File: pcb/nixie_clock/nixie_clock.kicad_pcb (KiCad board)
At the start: 4 copper layers, 0 parts

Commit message: schematic finalisation, footprint assignment and start on placeing components in layout.
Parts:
- added C1: 10u, Capacitor_SMD:C_1210_3225Metric, F.Cu at (165.8, 121.5)
- added C2: 100n, Capacitor_SMD:C_0805_2012Metric, F.Cu at (179.9, 124.5)
- added C3: 560p, Capacitor_SMD:C_0603_1608Metric, F.Cu at (161.0, 110.7)
- added C4: 150n, Capacitor_SMD:C_0603_1608Metric, F.Cu at (161.0, 113.2)
- added C5: 4u7, Capacitor_SMD:C_0603_1608Metric, F.Cu at (161.0, 115.8)
- added C6: 2u2, Capacitor_SMD:C_2220_5750Metric, F.Cu at (174.3, 113.0)
- added C7: 100n, Capacitor_SMD:C_1812_4532Metric, F.Cu at (166.5, 112.0)
- added C8: 10u, Capacitor_SMD:C_1210_3225Metric, F.Cu at (165.8, 125.8)
- added D1: D, Capacitor_SMD:C_1812_4532Metric, F.Cu at (166.5, 116.9)
- added Q1: Q_NMOS_GDS, Package_TO_SOT_SMD:LFPAK56, F.Cu at (174.3, 119.7)
- added R1: 7K87, Resistor_SMD:R_0603_1608Metric, F.Cu at (62.0, 84.6)
- added R10: 1K, Resistor_SMD:R_0603_1608Metric, F.Cu at (70.0, 87.1)
- added R11: 1K, Resistor_SMD:R_0603_1608Metric, F.Cu at (70.0, 89.6)
- added R12: 1K, Resistor_SMD:R_0603_1608Metric, F.Cu at (70.0, 92.1)
- added R13: 7K87, Resistor_SMD:R_0603_1608Metric, F.Cu at (84.3, 86.5)
- added R14: 1K, Resistor_SMD:R_0603_1608Metric, F.Cu at (84.3, 89.0)
- added R15: 1K, Resistor_SMD:R_0603_1608Metric, F.Cu at (84.3, 91.5)
- added R16: 1K, Resistor_SMD:R_0603_1608Metric, F.Cu at (84.3, 94.0)
- added R17: 1K, Resistor_SMD:R_0603_1608Metric, F.Cu at (88.3, 86.5)
- added R18: 1K, Resistor_SMD:R_0603_1608Metric, F.Cu at (88.3, 89.0)
- added R19: 7K87, Resistor_SMD:R_0603_1608Metric, F.Cu at (88.3, 91.5)
- added R2: 1K, Resistor_SMD:R_0603_1608Metric, F.Cu at (62.0, 87.1)
- added R20: 1K, Resistor_SMD:R_0603_1608Metric, F.Cu at (88.3, 94.0)
- added R21: 1K, Resistor_SMD:R_0603_1608Metric, F.Cu at (92.3, 86.5)
- added R22: 1K, Resistor_SMD:R_0603_1608Metric, F.Cu at (92.3, 89.0)
- added R23: 1K, Resistor_SMD:R_0603_1608Metric, F.Cu at (92.3, 91.5)
- added R24: 1K, Resistor_SMD:R_0603_1608Metric, F.Cu at (92.3, 94.0)
- added R25: 7K87, Resistor_SMD:R_0603_1608Metric, F.Cu at (105.8, 83.5)
- added R26: 1K, Resistor_SMD:R_0603_1608Metric, F.Cu at (105.8, 86.0)
- added R27: 1K, Resistor_SMD:R_0603_1608Metric, F.Cu at (105.8, 88.5)
- added R28: 1K, Resistor_SMD:R_0603_1608Metric, F.Cu at (105.8, 91.0)
- added R29: 1K, Resistor_SMD:R_0603_1608Metric, F.Cu at (109.8, 83.5)
- added R3: 1K, Resistor_SMD:R_0603_1608Metric, F.Cu at (62.0, 89.6)
- added R30: 1K, Resistor_SMD:R_0603_1608Metric, F.Cu at (109.8, 86.0)
- added R31: 7K87, Resistor_SMD:R_0603_1608Metric, F.Cu at (109.8, 88.5)
- added R32: 1K, Resistor_SMD:R_0603_1608Metric, F.Cu at (109.8, 91.0)
- added R33: 1K, Resistor_SMD:R_0603_1608Metric, F.Cu at (113.8, 83.5)
- added R34: 1K, Resistor_SMD:R_0603_1608Metric, F.Cu at (113.8, 86.0)
- added R35: 1K, Resistor_SMD:R_0603_1608Metric, F.Cu at (113.8, 88.5)
- added R36: 1K, Resistor_SMD:R_0603_1608Metric, F.Cu at (113.8, 91.0)
- added R37: 7K87, Resistor_SMD:R_0603_1608Metric, F.Cu at (129.0, 86.2)
- added R38: 1K, Resistor_SMD:R_0603_1608Metric, F.Cu at (129.0, 88.7)
- added R39: 1K, Resistor_SMD:R_0603_1608Metric, F.Cu at (129.0, 91.3)
- added R4: 1K, Resistor_SMD:R_0603_1608Metric, F.Cu at (62.0, 92.1)
- added R40: 1K, Resistor_SMD:R_0603_1608Metric, F.Cu at (129.0, 93.8)
- added R41: 1K, Resistor_SMD:R_0603_1608Metric, F.Cu at (133.0, 86.2)
- added R42: 1K, Resistor_SMD:R_0603_1608Metric, F.Cu at (133.0, 88.7)
- added R43: 7K87, Resistor_SMD:R_0603_1608Metric, F.Cu at (133.0, 91.3)
- added R44: 1K, Resistor_SMD:R_0603_1608Metric, F.Cu at (133.0, 93.8)
- added R45: 1K, Resistor_SMD:R_0603_1608Metric, F.Cu at (137.0, 86.2)
- added R46: 1K, Resistor_SMD:R_0603_1608Metric, F.Cu at (137.0, 88.7)
- added R47: 1K, Resistor_SMD:R_0603_1608Metric, F.Cu at (137.0, 91.3)
- added R48: 1K, Resistor_SMD:R_0603_1608Metric, F.Cu at (137.0, 93.8)
- added R49: 7K87, Resistor_SMD:R_0603_1608Metric, F.Cu at (152.0, 84.7)
- added R5: 1K, Resistor_SMD:R_0603_1608Metric, F.Cu at (66.0, 84.6)
- added R50: 1K, Resistor_SMD:R_0603_1608Metric, F.Cu at (152.0, 87.2)
- added R51: 1K, Resistor_SMD:R_0603_1608Metric, F.Cu at (152.0, 89.8)
- added R52: 1K, Resistor_SMD:R_0603_1608Metric, F.Cu at (152.0, 92.3)
- added R53: 1K, Resistor_SMD:R_0603_1608Metric, F.Cu at (156.0, 84.7)
- added R54: 1K, Resistor_SMD:R_0603_1608Metric, F.Cu at (156.0, 87.2)
- added R55: 7K87, Resistor_SMD:R_0603_1608Metric, F.Cu at (156.0, 89.8)
- added R56: 1K, Resistor_SMD:R_0603_1608Metric, F.Cu at (156.0, 92.3)
- added R57: 1K, Resistor_SMD:R_0603_1608Metric, F.Cu at (160.0, 84.7)
- added R58: 1K, Resistor_SMD:R_0603_1608Metric, F.Cu at (160.0, 87.2)
- added R59: 1K, Resistor_SMD:R_0603_1608Metric, F.Cu at (160.0, 89.8)
- added R6: 1K, Resistor_SMD:R_0603_1608Metric, F.Cu at (66.0, 87.1)
- added R60: 1K, Resistor_SMD:R_0603_1608Metric, F.Cu at (160.0, 92.3)
- added R61: 10m, Resistor_SMD:R_0805_2012Metric, F.Cu at (179.9, 127.5)
- added R62: 1M6, Resistor_SMD:R_0603_1608Metric, F.Cu at (161.0, 118.3)
- added R63: 13K, Resistor_SMD:R_0603_1608Metric, F.Cu at (161.0, 120.8)
- added R64: 20R, Resistor_SMD:R_0603_1608Metric, F.Cu at (161.0, 123.3)
- added R65: 300K, Resistor_SMD:R_0603_1608Metric, F.Cu at (161.0, 125.8)
- added R66: 7K87, Resistor_SMD:R_0603_1608Metric, F.Cu at (173.5, 44.0)
- added R67: 1K, Resistor_SMD:R_0603_1608Metric, F.Cu at (170.5, 45.5)
- added R68: 1K, Resistor_SMD:R_0603_1608Metric, F.Cu at (168.0, 49.5)
- added R69: 1K, Resistor_SMD:R_0603_1608Metric, F.Cu at (171.0, 63.5)
- added R7: 7K87, Resistor_SMD:R_0603_1608Metric, F.Cu at (66.0, 89.6)
- added R70: 1K, Resistor_SMD:R_0603_1608Metric, F.Cu at (174.5, 71.0)
- added R71: 1K, Resistor_SMD:R_0603_1608Metric, F.Cu at (179.5, 71.7)
- added R72: 86K6, Resistor_SMD:R_0603_1608Metric, F.Cu at (161.0, 128.3)
- added R73: 7K87, Resistor_SMD:R_0603_1608Metric, F.Cu at (180.3, 42.0)
- added R74: 1K, Resistor_SMD:R_0603_1608Metric, F.Cu at (187.0, 43.3)
- added R75: 1K, Resistor_SMD:R_0603_1608Metric, F.Cu at (191.0, 46.5)
- added R76: 1K, Resistor_SMD:R_0603_1608Metric, F.Cu at (190.0, 66.0)
- added R77: 1K, Resistor_SMD:R_0603_1608Metric, F.Cu at (187.0, 69.2)
- added R78: 1K, Resistor_SMD:R_0603_1608Metric, F.Cu at (183.5, 71.7)
- added R8: 1K, Resistor_SMD:R_0603_1608Metric, F.Cu at (66.0, 92.1)
- added R9: 1K, Resistor_SMD:R_0603_1608Metric, F.Cu at (70.0, 84.6)
- added T1: 750312367, 750312367:750312367, F.Cu at (170.3, 102.8)
- added U1: MSD42WT1G, footprints:SOT-323-3_2P2X1P35_ONS, F.Cu at (62.0, 69.6)
- added U10: MSD42WT1G, footprints:SOT-323-3_2P2X1P35_ONS, F.Cu at (65.8, 80.4)
- added U11: MSD42WT1G, footprints:SOT-323-3_2P2X1P35_ONS, F.Cu at (69.7, 80.4)
- added U12: MSD42WT1G, footprints:SOT-323-3_2P2X1P35_ONS, F.Cu at (73.6, 80.4)
- added U13: PCA9685BS, Package_DFN_QFN:QFN-28-1EP_6x6mm_P0.65mm_EP4.25x4.25mm, F.Cu at (237.1, 129.7)
- added U14: PicoW, RPi_Pico:RPi_PicoW_SMD, F.Cu at (71.0, 127.5)
- added U15: PCA9685BS, Package_DFN_QFN:QFN-28-1EP_6x6mm_P0.65mm_EP4.25x4.25mm, F.Cu at (226.8, 129.7)
- added U16: MSD42WT1G, footprints:SOT-323-3_2P2X1P35_ONS, F.Cu at (84.3, 71.5)
- added U17: MSD42WT1G, footprints:SOT-323-3_2P2X1P35_ONS, F.Cu at (88.1, 71.5)
- added U18: MSD42WT1G, footprints:SOT-323-3_2P2X1P35_ONS, F.Cu at (92.0, 71.5)
- added U19: MSD42WT1G, footprints:SOT-323-3_2P2X1P35_ONS, F.Cu at (95.9, 71.5)
- added U2: MSD42WT1G, footprints:SOT-323-3_2P2X1P35_ONS, F.Cu at (65.8, 69.6)
- added U20: MSD42WT1G, footprints:SOT-323-3_2P2X1P35_ONS, F.Cu at (84.3, 76.9)
- added U21: MSD42WT1G, footprints:SOT-323-3_2P2X1P35_ONS, F.Cu at (88.1, 76.9)
- added U22: MSD42WT1G, footprints:SOT-323-3_2P2X1P35_ONS, F.Cu at (92.0, 76.9)
- added U23: MSD42WT1G, footprints:SOT-323-3_2P2X1P35_ONS, F.Cu at (95.9, 76.9)
- added U24: MSD42WT1G, footprints:SOT-323-3_2P2X1P35_ONS, F.Cu at (84.3, 82.2)
- added U25: MSD42WT1G, footprints:SOT-323-3_2P2X1P35_ONS, F.Cu at (88.1, 82.2)
- added U26: MSD42WT1G, footprints:SOT-323-3_2P2X1P35_ONS, F.Cu at (92.0, 82.2)
- added U27: MSD42WT1G, footprints:SOT-323-3_2P2X1P35_ONS, F.Cu at (95.9, 82.2)
- added U28: PCA9685BS, Package_DFN_QFN:QFN-28-1EP_6x6mm_P0.65mm_EP4.25x4.25mm, F.Cu at (199.5, 129.7)
- added U29: MSD42WT1G, footprints:SOT-323-3_2P2X1P35_ONS, F.Cu at (105.7, 68.5)
- added U3: MSD42WT1G, footprints:SOT-323-3_2P2X1P35_ONS, F.Cu at (69.7, 69.6)
- added U30: MSD42WT1G, footprints:SOT-323-3_2P2X1P35_ONS, F.Cu at (109.6, 68.5)
- added U31: MSD42WT1G, footprints:SOT-323-3_2P2X1P35_ONS, F.Cu at (113.5, 68.5)
- added U32: MSD42WT1G, footprints:SOT-323-3_2P2X1P35_ONS, F.Cu at (117.3, 68.5)
- added U33: MSD42WT1G, footprints:SOT-323-3_2P2X1P35_ONS, F.Cu at (105.7, 73.9)
- added U34: MSD42WT1G, footprints:SOT-323-3_2P2X1P35_ONS, F.Cu at (109.6, 73.9)
- added U35: MSD42WT1G, footprints:SOT-323-3_2P2X1P35_ONS, F.Cu at (113.5, 73.9)
- added U36: MSD42WT1G, footprints:SOT-323-3_2P2X1P35_ONS, F.Cu at (117.3, 73.9)
- added U37: MSD42WT1G, footprints:SOT-323-3_2P2X1P35_ONS, F.Cu at (105.7, 79.3)
- added U38: MSD42WT1G, footprints:SOT-323-3_2P2X1P35_ONS, F.Cu at (109.6, 79.3)
- added U39: MSD42WT1G, footprints:SOT-323-3_2P2X1P35_ONS, F.Cu at (113.5, 79.3)
- added U4: MSD42WT1G, footprints:SOT-323-3_2P2X1P35_ONS, F.Cu at (73.6, 69.6)
- added U40: MSD42WT1G, footprints:SOT-323-3_2P2X1P35_ONS, F.Cu at (117.3, 79.3)
- added U41: PCA9685BS, Package_DFN_QFN:QFN-28-1EP_6x6mm_P0.65mm_EP4.25x4.25mm, F.Cu at (189.2, 129.7)
- added U42: MSD42WT1G, footprints:SOT-323-3_2P2X1P35_ONS, F.Cu at (129.0, 71.3)
- added U43: MSD42WT1G, footprints:SOT-323-3_2P2X1P35_ONS, F.Cu at (132.8, 71.3)
- added U44: MSD42WT1G, footprints:SOT-323-3_2P2X1P35_ONS, F.Cu at (136.7, 71.3)
- added U45: MSD42WT1G, footprints:SOT-323-3_2P2X1P35_ONS, F.Cu at (140.6, 71.3)
- added U46: MSD42WT1G, footprints:SOT-323-3_2P2X1P35_ONS, F.Cu at (129.0, 76.6)
- added U47: MSD42WT1G, footprints:SOT-323-3_2P2X1P35_ONS, F.Cu at (132.8, 76.6)
- added U48: MSD42WT1G, footprints:SOT-323-3_2P2X1P35_ONS, F.Cu at (136.7, 76.6)
- added U49: MSD42WT1G, footprints:SOT-323-3_2P2X1P35_ONS, F.Cu at (140.6, 76.6)
- added U5: MSD42WT1G, footprints:SOT-323-3_2P2X1P35_ONS, F.Cu at (62.0, 75.0)
- added U50: MSD42WT1G, footprints:SOT-323-3_2P2X1P35_ONS, F.Cu at (129.0, 82.0)
- added U51: MSD42WT1G, footprints:SOT-323-3_2P2X1P35_ONS, F.Cu at (132.8, 82.0)
- added U52: MSD42WT1G, footprints:SOT-323-3_2P2X1P35_ONS, F.Cu at (136.7, 82.0)
- added U53: MSD42WT1G, footprints:SOT-323-3_2P2X1P35_ONS, F.Cu at (140.6, 82.0)
- added U54: PCA9685BS, Package_DFN_QFN:QFN-28-1EP_6x6mm_P0.65mm_EP4.25x4.25mm, F.Cu at (209.8, 129.7)
- added U55: MSD42WT1G, footprints:SOT-323-3_2P2X1P35_ONS, F.Cu at (152.0, 69.8)
- added U56: MSD42WT1G, footprints:SOT-323-3_2P2X1P35_ONS, F.Cu at (155.8, 69.8)
- added U57: MSD42WT1G, footprints:SOT-323-3_2P2X1P35_ONS, F.Cu at (159.7, 69.8)
- added U58: MSD42WT1G, footprints:SOT-323-3_2P2X1P35_ONS, F.Cu at (163.6, 69.8)
- added U59: MSD42WT1G, footprints:SOT-323-3_2P2X1P35_ONS, F.Cu at (152.0, 75.1)
- added U6: MSD42WT1G, footprints:SOT-323-3_2P2X1P35_ONS, F.Cu at (65.8, 75.0)
- added U60: MSD42WT1G, footprints:SOT-323-3_2P2X1P35_ONS, F.Cu at (155.8, 75.1)
- added U61: MSD42WT1G, footprints:SOT-323-3_2P2X1P35_ONS, F.Cu at (159.7, 75.1)
- added U62: MSD42WT1G, footprints:SOT-323-3_2P2X1P35_ONS, F.Cu at (163.6, 75.1)
- added U63: MSD42WT1G, footprints:SOT-323-3_2P2X1P35_ONS, F.Cu at (152.0, 80.5)
- added U64: MSD42WT1G, footprints:SOT-323-3_2P2X1P35_ONS, F.Cu at (155.8, 80.5)
- added U65: MSD42WT1G, footprints:SOT-323-3_2P2X1P35_ONS, F.Cu at (159.7, 80.5)
- added U66: MSD42WT1G, footprints:SOT-323-3_2P2X1P35_ONS, F.Cu at (177.3, 45.0)
- added U67: MSD42WT1G, footprints:SOT-323-3_2P2X1P35_ONS, F.Cu at (171.2, 49.0)
- added U68: MSD42WT1G, footprints:SOT-323-3_2P2X1P35_ONS, F.Cu at (168.7, 53.5)
- added U69: MSD42WT1G, footprints:SOT-323-3_2P2X1P35_ONS, F.Cu at (168.7, 60.0)
- added U7: MSD42WT1G, footprints:SOT-323-3_2P2X1P35_ONS, F.Cu at (69.7, 75.0)
- added U70: MSD42WT1G, footprints:SOT-323-3_2P2X1P35_ONS, F.Cu at (173.7, 67.0)
- added U71: MSD42WT1G, footprints:SOT-323-3_2P2X1P35_ONS, F.Cu at (178.7, 68.0)
- added U72: MSD42WT1G, footprints:SOT-323-3_2P2X1P35_ONS, F.Cu at (183.5, 45.0)
- added U73: MSD42WT1G, footprints:SOT-323-3_2P2X1P35_ONS, F.Cu at (187.7, 47.5)
- added U74: MSD42WT1G, footprints:SOT-323-3_2P2X1P35_ONS, F.Cu at (191.2, 51.0)
- added U75: MSD42WT1G, footprints:SOT-323-3_2P2X1P35_ONS, F.Cu at (189.3, 62.0)
- added U76: MSD42WT1G, footprints:SOT-323-3_2P2X1P35_ONS, F.Cu at (186.3, 65.0)
- added U77: MSD42WT1G, footprints:SOT-323-3_2P2X1P35_ONS, F.Cu at (182.3, 68.0)
- added U78: MSD42WT1G, footprints:SOT-323-3_2P2X1P35_ONS, F.Cu at (163.6, 80.5)
- added U79: LT3759EMSE-TRPBF, LT3759EMSE:MSOP-12_MSE_LIT, F.Cu at (173.8, 125.9)
- added U8: MSD42WT1G, footprints:SOT-323-3_2P2X1P35_ONS, F.Cu at (73.6, 75.0)
- added U9: MSD42WT1G, footprints:SOT-323-3_2P2X1P35_ONS, F.Cu at (62.0, 80.4)
- added V1: IN14, Nixie_Stuff:IN14, B.Cu at (66.8, 57.7)
- added V2: IN14, Nixie_Stuff:IN14, B.Cu at (88.9, 57.5)
- added V3: IN14, Nixie_Stuff:IN14, B.Cu at (108.9, 56.5)
- added V4: IN14, Nixie_Stuff:IN14, B.Cu at (134.1, 56.5)
- added V5: IN14, Nixie_Stuff:IN14, B.Cu at (156.0, 56.2)
- added V6: IN14, Nixie_Stuff:IN14, B.Cu at (180.0, 56.0)

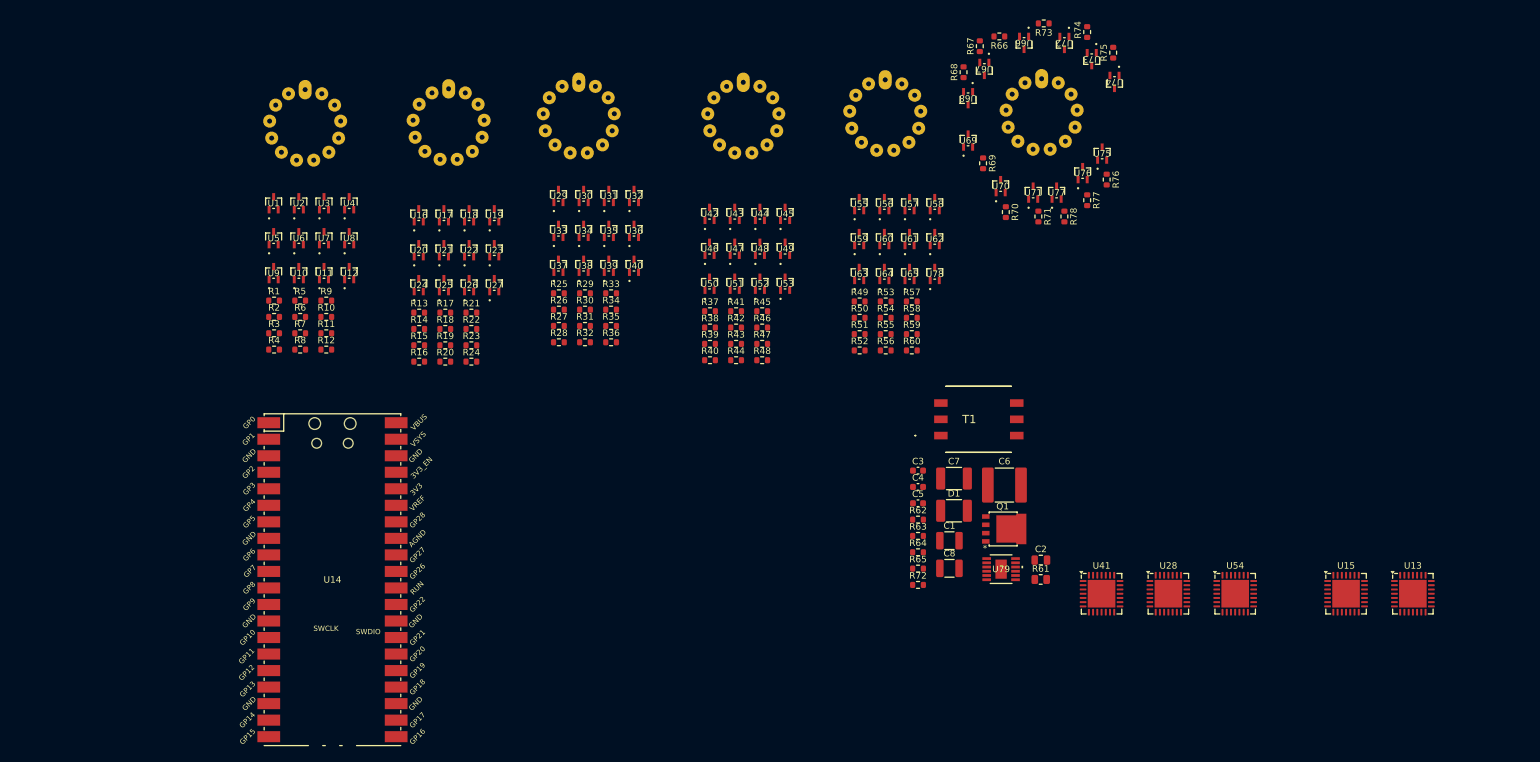
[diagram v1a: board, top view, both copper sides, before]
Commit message: finalization of schematic (might add fuze on 170v supply) looking at pcb routing now. Decided on 6 layers.
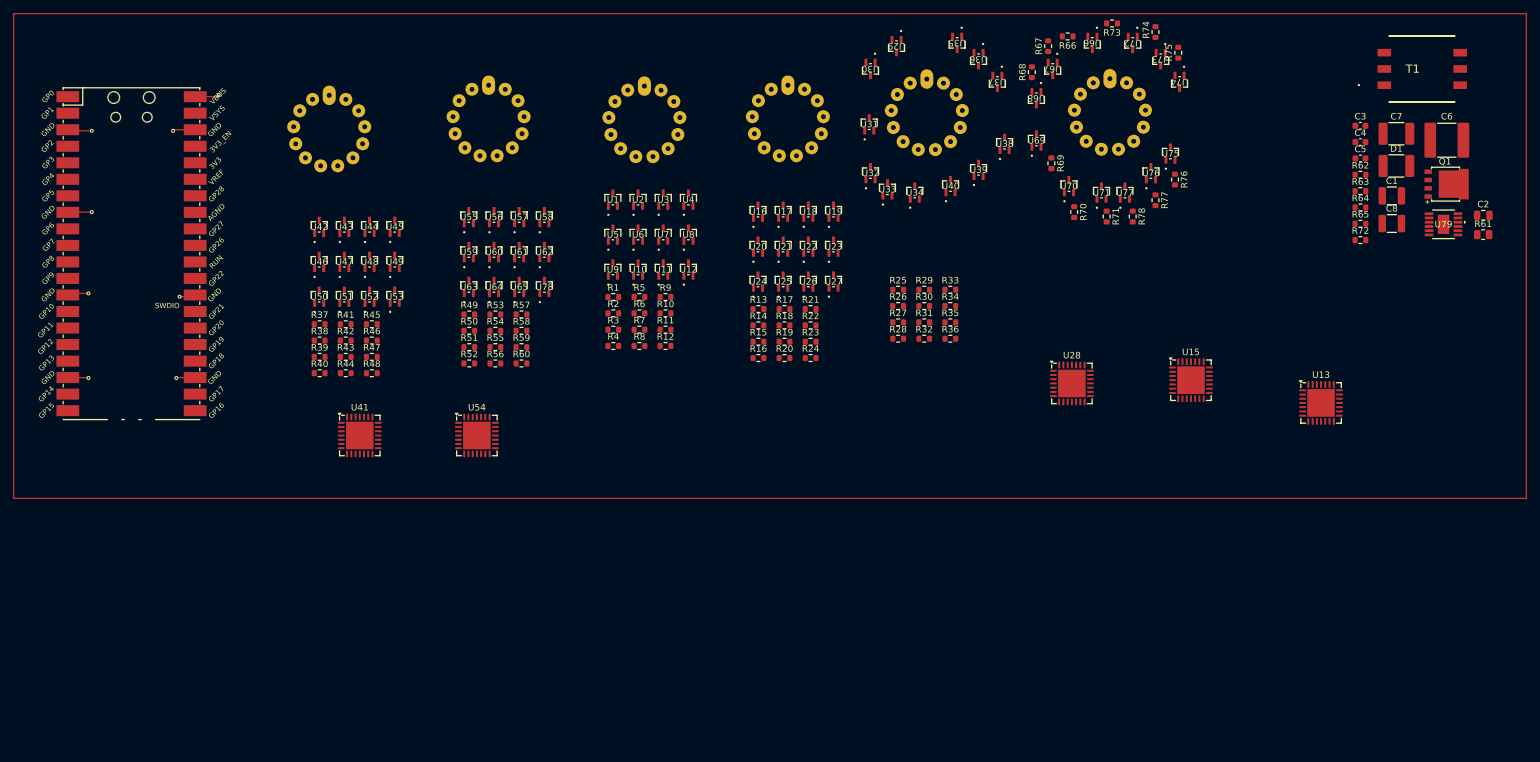
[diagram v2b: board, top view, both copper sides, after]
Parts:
- moved U54 119.1 mm to (93.2, 105.3)
- moved U41 116.6 mm to (75.2, 105.3)
- moved T1 86.9 mm to (238.5, 49.0)
- moved C1 86.2 mm to (233.8, 68.5)
- moved C2 86.2 mm to (247.9, 71.5)
- moved C3 86.2 mm to (229.0, 57.7)
- moved C4 86.2 mm to (229.0, 60.2)
- moved C5 86.2 mm to (229.0, 62.8)
- moved C6 86.2 mm to (242.3, 60.0)
- moved C7 86.2 mm to (234.5, 59.0)
- moved C8 86.2 mm to (233.8, 72.8)
- moved D1 86.2 mm to (234.5, 63.9)
- moved Q1 86.2 mm to (242.3, 66.7)
- moved R61 86.2 mm to (247.9, 74.5)
- moved R62 86.2 mm to (229.0, 65.3)
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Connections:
- U14 pad 40: Net-(U14-VBUS) -> +5V
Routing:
- net GND: track 0.00 -> 100.2 mm, vias 0 -> 7
- net +5V: track 0.00 -> 4.61 mm, vias 0 -> 1
- added copper zone on In3.Cu, net +170V
- added copper zone on In2.Cu, net +5V
- added copper zone on In1.Cu, net GND
- added copper zone on In4.Cu, net GND
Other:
- copper layers 4 -> 6

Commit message: hierarkical pcb switch and finishing of layout time for final checks need to redo nixie tube layout
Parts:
- moved R75 146.1 mm to (68.6, 108.3), turned to -90 degrees
- moved R74 143.8 mm to (71.6, 112.8), turned to -90 degrees
- moved U74 143.7 mm to (67.9, 104.6), turned to 0 degrees
- moved U73 141.3 mm to (70.9, 108.6), turned to 0 degrees
- moved U72 136.8 mm to (73.9, 110.6), turned to 0 degrees
- moved R73 136.8 mm to (74.7, 114.3), turned to -90 degrees
- moved R76 133.8 mm to (68.6, 88.8), turned to 90 degrees
- moved U75 133.8 mm to (69.4, 92.1), turned to 180 degrees
- moved R51 128.2 mm to (219.1, 108.3), turned to -90 degrees
- moved U55 127.4 mm to (213.4, 110.1)
- moved R50 127.1 mm to (217.1, 111.8), turned to -90 degrees
- moved R77 127.0 mm to (71.6, 86.3), turned to 90 degrees
- moved R39 127.0 mm to (195.1, 108.3), turned to -90 degrees
- moved U76 126.8 mm to (72.4, 89.6), turned to 180 degrees
- moved U42 126.0 mm to (189.4, 110.1)
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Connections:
- R62 pad 2: Net-(D1-A) -> +170V
- U13 pad 27: GND -> +5V
- U15 pad 26: GND -> +5V
- U15 pad 27: +5V -> GND
- U28 pad 26: +5V -> GND
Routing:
- net /Nixie_Control/Ext_Clk: track 0.00 -> 211.9 mm, vias 0 -> 6
- net /Nixie_Boost/HV_EN: track 0.00 -> 190.7 mm, vias 0 -> 2
- net /Nixie_Control/SDA: track 0.00 -> 182.3 mm
- net /Nixie_Control/SCL: track 0.00 -> 177.8 mm, vias 0 -> 6
- net GND: track 100.2 -> 241.6 mm, vias 7 -> 121
- net /Nixie_Block1/Cath_3: track 0.00 -> 115.2 mm, vias 0 -> 2
- net /Nixie_Block1/Cath_2: track 0.00 -> 98.7 mm, vias 0 -> 2
- net /Nixie_Block1/Cath_1: track 0.00 -> 94.2 mm, vias 0 -> 2
- net /Nixie_Block1/Cath_0: track 0.00 -> 77.0 mm, vias 0 -> 2
- net /Nixie_Block1/Cath_8: track 0.00 -> 63.0 mm, vias 0 -> 2
- net /Nixie_Block1/Comma_L: track 0.00 -> 61.8 mm, vias 0 -> 2
- net /Nixie_Block1/Comma_R: track 0.00 -> 59.9 mm, vias 0 -> 2
- net /Nixie_Block1/Cath_9: track 0.00 -> 58.2 mm, vias 0 -> 2
- net /Nixie_Block1/Cath_4: track 0.00 -> 49.1 mm, vias 0 -> 2
- net /Nixie_Block1/Cath_5: track 0.00 -> 47.7 mm, vias 0 -> 2
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- added copper zone on F.Cu, net Net-(Q1-D)
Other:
- board outline added: 236.2 x 53.3 mm

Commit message: 3d models done
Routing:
- net GND: track 241.6 -> 229.1 mm, vias 121 -> 126
- net Net-(Q1-S): track 13.2 -> 13.7 mm

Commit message: fixing some issues.
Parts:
- D1: footprint Capacitor_SMD:C_1812_4532Metric -> Diode_SMD:D_SOD-123
- U79: value LT3759EMSE-TRPBF -> LT3759EMSE#TRPBF
- moved D1 0.56 mm to (232.5, 114.3)
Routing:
- net GND: track 229.1 -> 262.8 mm, vias 126 -> 130
- net +170V: track 12.5 -> 21.3 mm, vias 9 -> 5
- net +5V: track 28.3 -> 34.9 mm
- net Net-(Q1-G): track 3.40 -> 4.56 mm
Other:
- board size 236.2 x 53.3 mm -> 218.6 x 53.3 mm
- board text added: "JLCJLCJLCJLC"

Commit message: added grounding
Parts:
- added J1: Conn_01x06_Pin, Connector_Molex:Molex_KK-254_AE-6410-06A_1x06_P2.54mm_Vertical, F.Cu at (179.3, 124.8)
- moved C1 16.4 mm to (253.5, 88.9)
- moved C2 16.4 mm to (253.3, 91.5)
- moved C3 16.4 mm to (238.8, 100.4)
- moved C4 16.4 mm to (241.8, 99.1)
- moved C5 16.4 mm to (251.2, 118.8)
- moved C6 16.4 mm to (251.6, 122.7)
- moved C7 16.4 mm to (239.8, 86.6)
- moved C8 16.4 mm to (253.5, 85.6)
- moved D1 16.4 mm to (248.9, 114.2)
- moved Q1 16.4 mm to (247.6, 89.0)
- moved R1 16.4 mm to (177.5, 113.4)
- moved R10 16.4 mm to (162.0, 88.6)
- moved R11 16.4 mm to (165.0, 86.1)
- moved R12 16.4 mm to (168.5, 85.1)
- moved R13 16.4 mm to (124.5, 113.4)
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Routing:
- net GND: track 262.8 -> 235.4 mm, vias 130 -> 127
- net +5V: track 34.9 -> 29.3 mm
- net /Nixie_Boost/HV_EN: track 190.7 -> 191.6 mm
- net /Nixie_Control1/Nixie_Block2/Cath_6: track 34.6 -> 35.2 mm
- net /Nixie_Control4/Nixie_Block2/Cath_6: track 34.6 -> 35.2 mm
- net /Nixie_Control3/Nixie_Block2/Cath_6: track 34.6 -> 35.2 mm
- net /Nixie_Control2/Nixie_Block2/Cath_6: track 34.6 -> 35.2 mm
- net /Nixie_Control/Nixie_Block2/Cath_6: track 34.6 -> 35.2 mm
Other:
- board size 218.6 x 53.3 mm -> 218.5 x 53.2 mm
